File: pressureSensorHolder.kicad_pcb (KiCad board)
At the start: 2 copper layers, 29.5 x 31 mm, 6 parts, among them J1 Conn_01x04, U1 SDP8xx-ANALOG

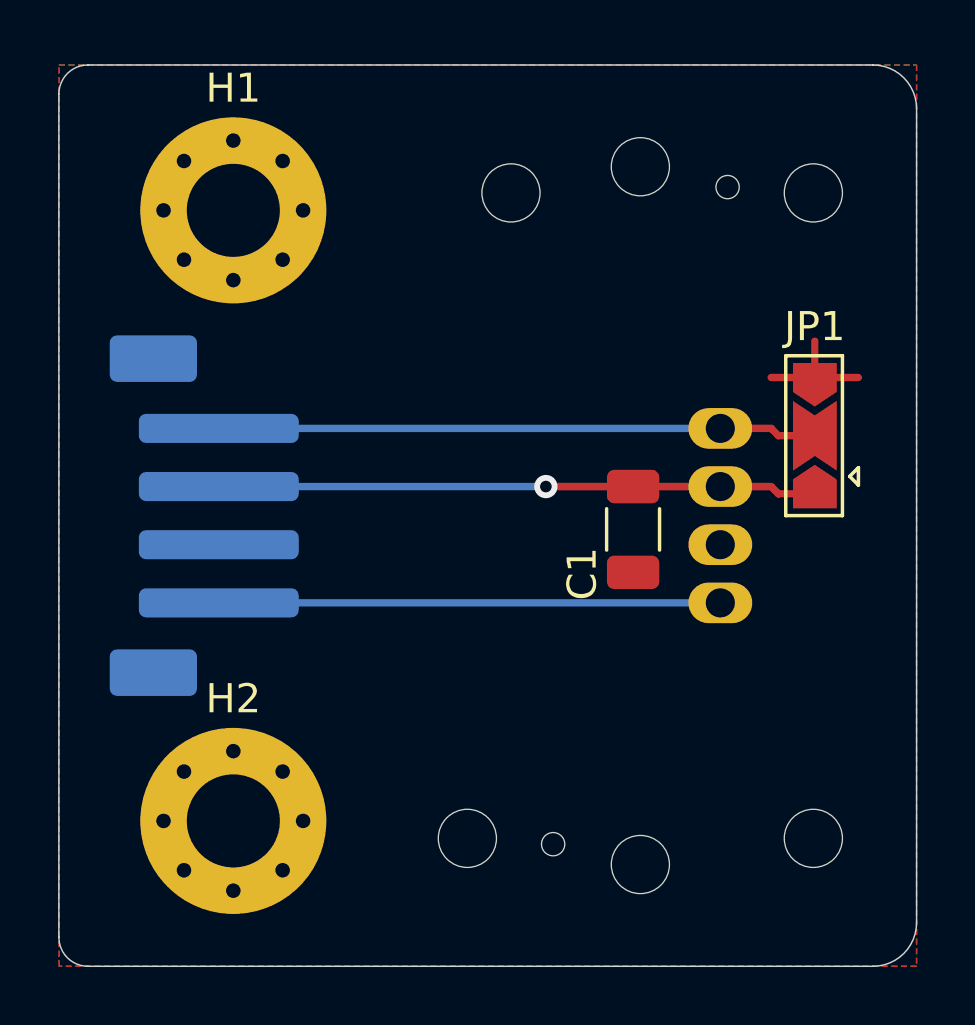
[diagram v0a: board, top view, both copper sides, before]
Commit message: Finished version for small minion housing
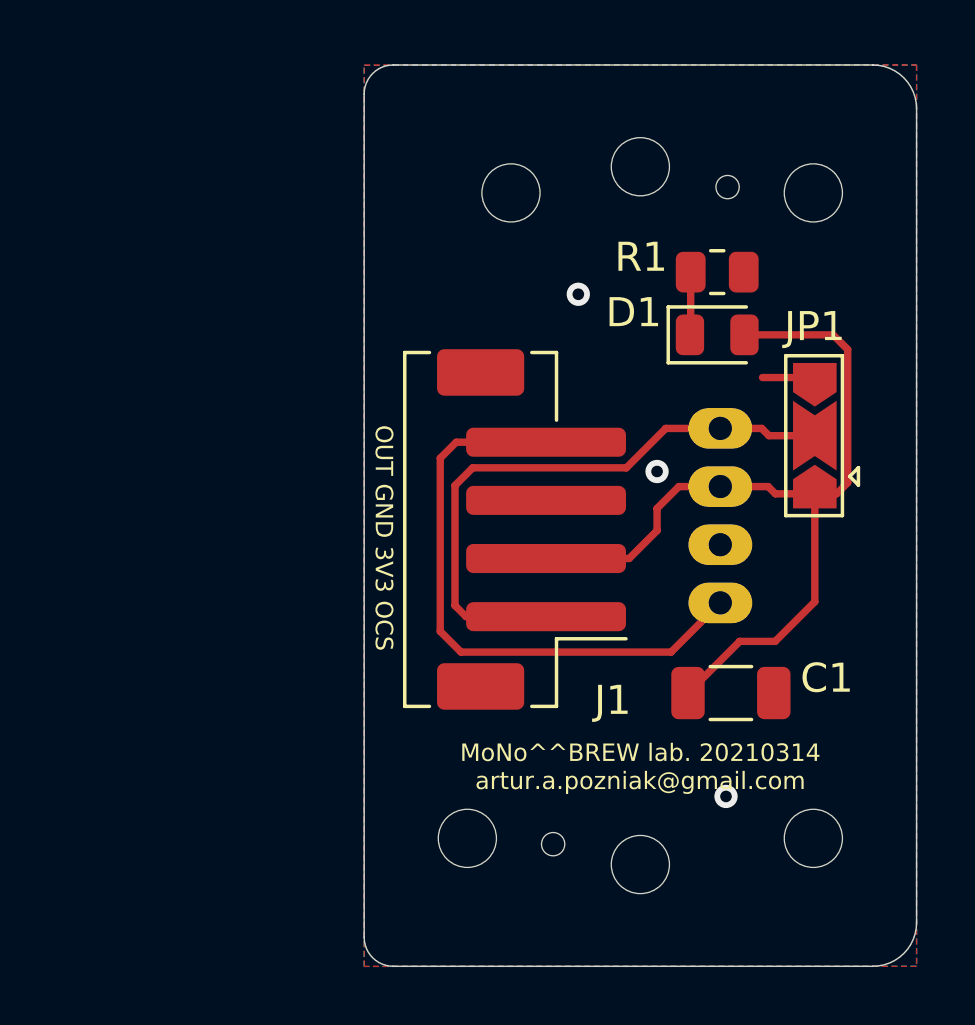
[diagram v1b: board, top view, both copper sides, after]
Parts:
- removed H1, H2: MountingHole, MountingHole:MountingHole_3.2mm_M3_Pad_Via
- added D1: LED, LED_SMD:LED_0805_2012Metric, F.Cu at (151.6, 77.4)
- added R1: 150R, Resistor_SMD:R_0805_2012Metric, F.Cu at (151.6, 75.3)
- J1: moved to F.Cu
- moved J1 11.3 mm to (145.2, 84.1), turned to 90 degrees
- moved C1 6.56 mm to (152.1, 89.8), turned to 0 degrees
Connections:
- net /Vdd renamed +3V3
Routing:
- net +3V3: track 20.6 -> 29.8 mm, vias 1 -> 0
- net /AOut_SDA: track 17.2 -> 20.5 mm
- net GND: track 4.25 -> 1.80 mm, vias 0 -> 3
- net Net-(D1-Pad1): track 0.00 -> 2.17 mm
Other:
- board size 29.5 x 31 mm -> 19 x 31 mm
- board text added: "MoNo^^BREW lab. 20210314 artur.a.pozniak@gmail.com"
- board text added: "OUT GND 3V3 OCS"
